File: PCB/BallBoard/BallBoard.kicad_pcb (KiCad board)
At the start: 2 copper layers, 24 x 13 mm, 5 parts, among them IC1 S7136, J1 side_l

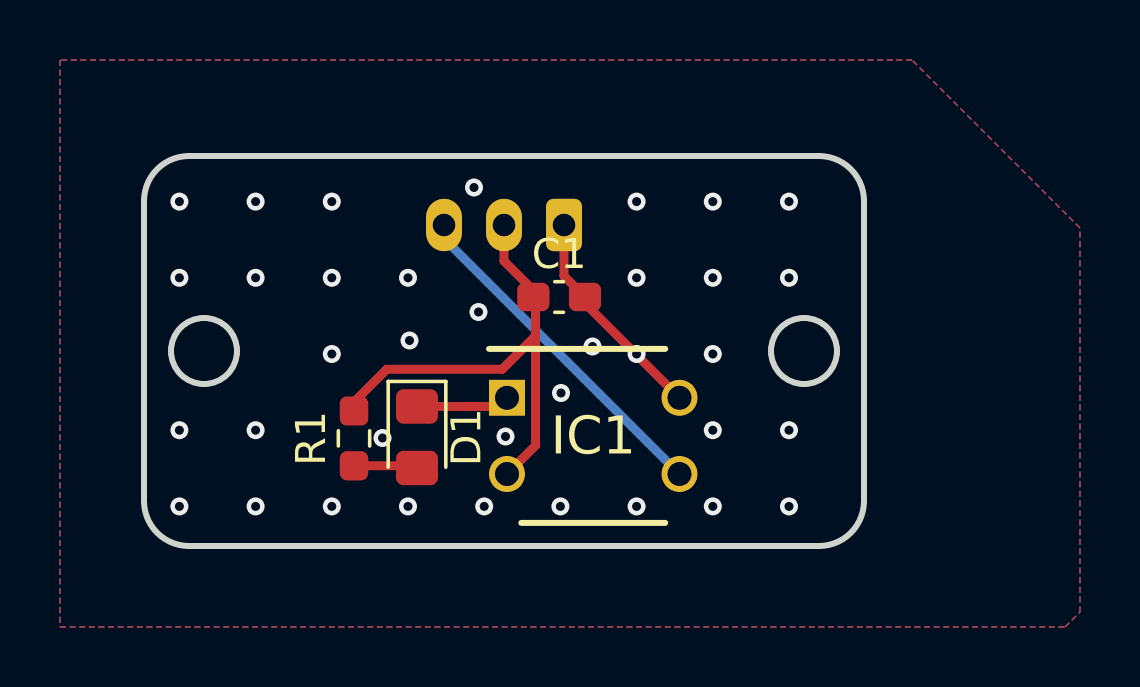
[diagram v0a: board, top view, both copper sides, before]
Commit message: オプション分圧抵抗追加
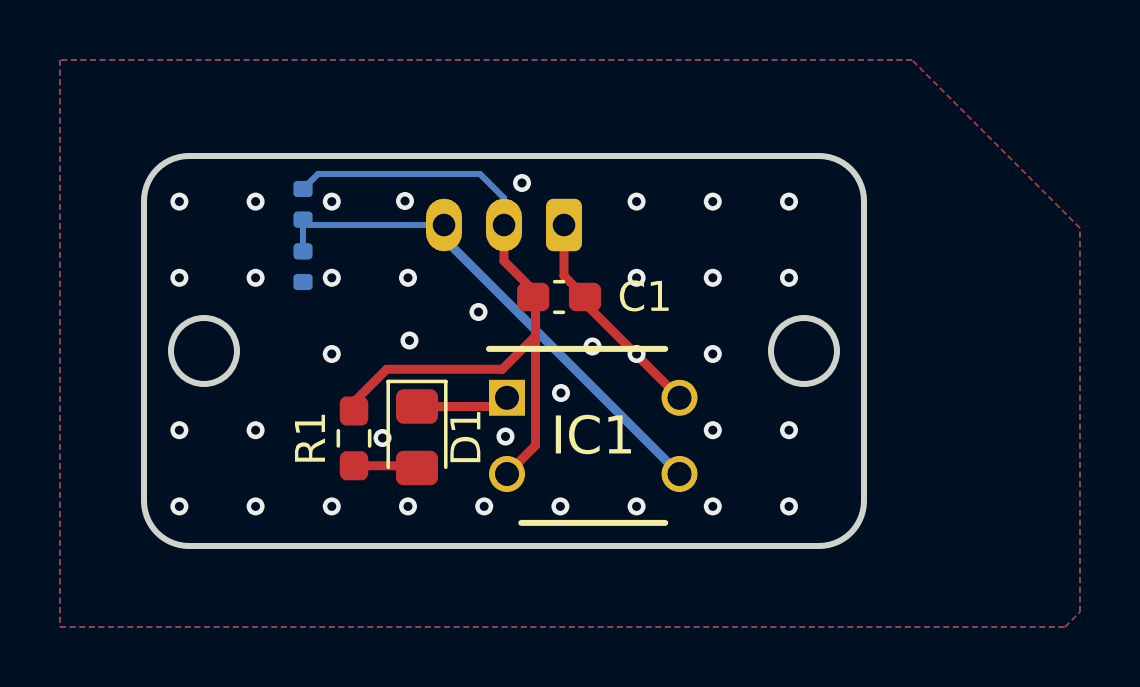
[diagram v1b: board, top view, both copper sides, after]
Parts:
- added R2: 5.6k, Resistor_SMD:R_0402_1005Metric, B.Cu at (60.0, 33.1)
- added R3: 10k, Resistor_SMD:R_0402_1005Metric, B.Cu at (60.0, 35.2)
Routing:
- net +5V: track 17.6 -> 25.8 mm
- net Net-(IC1-VOUT): track 11.6 -> 17.4 mm
- net GND: vias 36 -> 37
